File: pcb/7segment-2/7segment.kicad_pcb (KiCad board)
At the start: 2 copper layers, 26.4 x 21.8 mm, 3 parts, among them P1 CONN_02X05

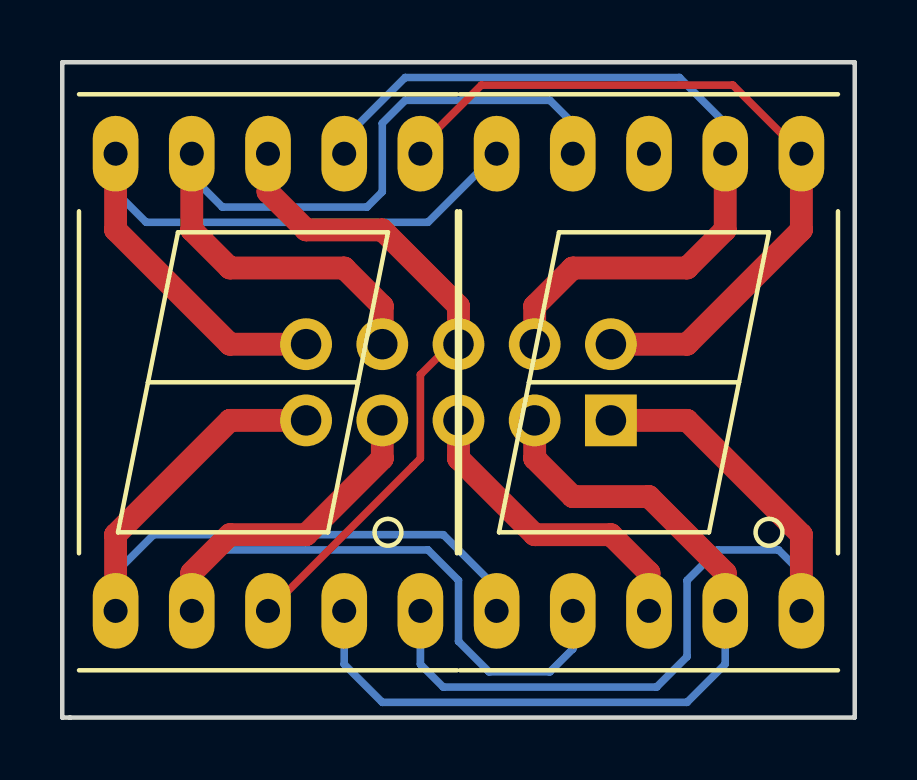
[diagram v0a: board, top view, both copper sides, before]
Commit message: added pinout to 7-segment pcb
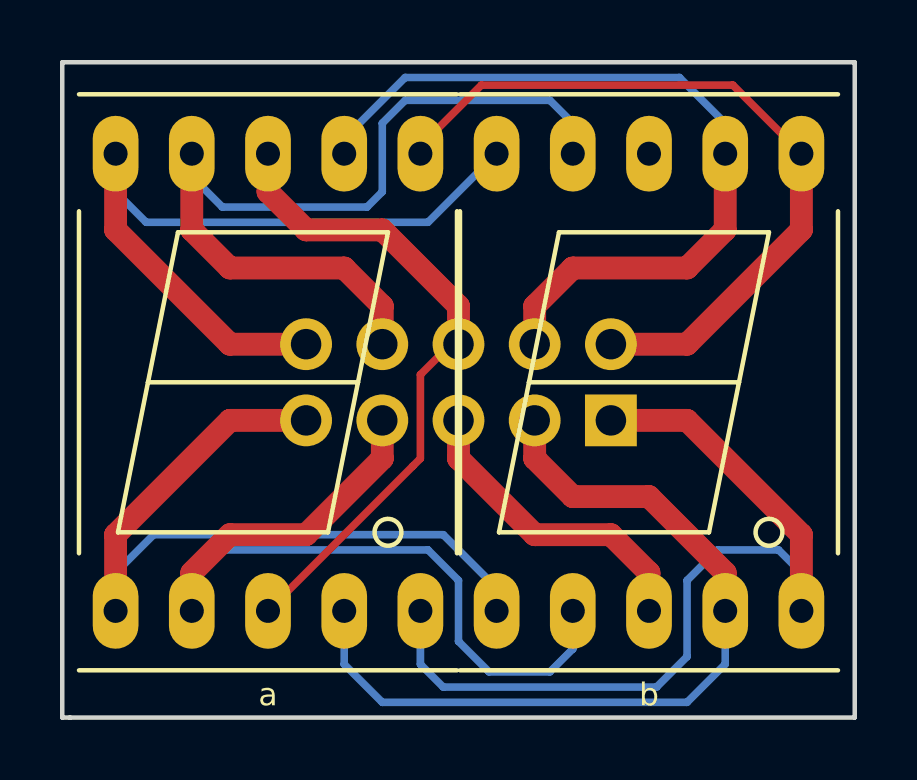
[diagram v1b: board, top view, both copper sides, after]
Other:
- board text added: "1 - dp"
- board text added: "10- g"
- board text added: "2 - b"
- board text added: "3 - c"
- board text added: "4 - a"
- board text added: "5 - se1"
- board text added: "6 - se2"
- board text added: "7 - d"
- board text added: "8 - f"
- board text added: "9 - e"
- board text added: "a"
- board text added: "b"
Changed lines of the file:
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@@
-(kicad_pcb (version 4) (host pcbnew 4.0.2+e4-6225~38~ubuntu14.04.1-stable)
+(kicad_pcb (version 4) (host pcbnew 4.0.4+e1-6308~48~ubuntu14.04.1-stable)
   (general
     (links 20)
     (no_connects 1)
-    (area 104.033095 93.396999 135.203001 117.115)
+    (area 104.108095 93.396999 135.203001 117.215)
     (thickness 1.6)
-    (drawings 5)
+    (drawings 17)
     (tracks 98)
     (zones 0)
@@
   )
   (setup
-    (last_trace_width 0.254)
+    (last_trace_width 0.25)
     (user_trace_width 0.254)
     (user_trace_width 0.508)
@@
     )
   )
+  (gr_text b (at 128.27 114.554) (layer F.SilkS)
+    (effects (font (size 0.762 0.762) (thickness 0.1905)))
+  )
+  (gr_text a (at 115.57 114.554) (layer F.SilkS)
+    (effects (font (size 0.762 0.762) (thickness 0.1905)))
+  )
+  (gr_text "10- g" (at 115.316 95.631) (layer B.SilkS)
+    (effects (font (size 1.016 1.016) (thickness 0.254)) (justify left mirror))
+  )
+  (gr_text "9 - e" (at 115.316 97.536) (layer B.SilkS)
+    (effects (font (size 1.016 1.016) (thickness 0.254)) (justify left mirror))
+  )
+  (gr_text "8 - f" (at 115.316 99.441) (layer B.SilkS)
+    (effects (font (size 1.016 1.016) (thickness 0.254)) (justify left mirror))
+  )
+  (gr_text "7 - d" (at 115.316 101.346) (layer B.SilkS)
+    (effects (font (size 1.016 1.016) (thickness 0.254)) (justify left mirror))
+  )
+  (gr_text "6 - se2" (at 115.316 103.251) (layer B.SilkS)
+    (effects (font (size 1.016 1.016) (thickness 0.254)) (justify left mirror))
+  )
+  (gr_text "5 - se1" (at 115.316 105.156) (layer B.SilkS)
+    (effects (font (size 1.016 1.016) (thickness 0.254)) (justify left mirror))
+  )
+  (gr_text "4 - a" (at 115.316 107.061) (layer B.SilkS)
+    (effects (font (size 1.016 1.016) (thickness 0.254)) (justify left mirror))
+  )
+  (gr_text "3 - c" (at 115.316 108.966) (layer B.SilkS)
+    (effects (font (size 1.016 1.016) (thickness 0.254)) (justify left mirror))
+  )
+  (gr_text "2 - b" (at 115.316 110.871) (layer B.SilkS)
+    (effects (font (size 1.016 1.016) (thickness 0.254)) (justify left mirror))
+  )
+  (gr_text "1 - dp" (at 115.316 112.776) (layer B.SilkS)
+    (effects (font (size 1.016 1.016) (thickness 0.254)) (justify left mirror))
+  )
   (gr_line (start 108.712 115.316) (end 108.712 93.472) (angle 90) (layer Edge.Cuts) (width 0.15))
   (gr_line (start 108.966 115.316) (end 108.712 115.316) (angle 90) (layer Edge.Cuts) (width 0.15))
@@
   (segment (start 116.84 109.22) (end 114.3 109.22) (width 0.762) (layer F.Cu) (net 2))
   (segment (start 119.38 106.68) (end 116.84 109.22) (width 0.762) (layer F.Cu) (net 2))
-  (via (at 115.57 111.76) (size 0.6) (drill 0.4) (layers F.Cu B.Cu) (net 3) (status C00000))
-  (segment (start 115.57 111.76) (end 120.396 106.934) (width 0.254) (layer F.Cu) (net 3) (status 400000))
-  (segment (start 120.65 103.886) (end 121.666 102.87) (width 0.254) (layer F.Cu) (net 3) (status 800000))
+  (via (at 115.57 111.76) (size 0.6) (drill 0.4) (layers F.Cu B.Cu) (net 3))
+  (segment (start 115.57 111.76) (end 120.396 106.934) (width 0.254) (layer F.Cu) (net 3))
+  (segment (start 120.65 103.886) (end 121.666 102.87) (width 0.254) (layer F.Cu) (net 3))
   (segment (start 120.65 106.68) (end 120.65 103.886) (width 0.254) (layer F.Cu) (net 3))
   (segment (start 120.396 106.934) (end 120.65 106.68) (width 0.254) (layer F.Cu) (net 3))
-  (segment (start 121.666 102.87) (end 121.92 102.87) (width 0.254) (layer F.Cu) (net 3) (status C00000))
+  (segment (start 121.666 102.87) (end 121.92 102.87) (width 0.254) (layer F.Cu) (net 3))
   (segment (start 121.92 102.87) (end 121.92 101.6) (width 0.762) (layer F.Cu) (net 3))
   (segment (start 115.57 97.79) (end 115.57 96.52) (width 0.762) (layer F.Cu) (net 3))
@@
   (segment (start 119.38 99.06) (end 116.84 99.06) (width 0.762) (layer F.Cu) (net 3))
   (segment (start 121.92 101.6) (end 119.38 99.06) (width 0.762) (layer F.Cu) (net 3))
-  (segment (start 118.11 111.76) (end 118.11 113.538) (width 0.254) (layer B.Cu) (net 4) (status 400000))
-  (segment (start 130.81 113.538) (end 130.81 111.76) (width 0.254) (layer B.Cu) (net 4) (status 800000))
+  (segment (start 118.11 111.76) (end 118.11 113.538) (width 0.254) (layer B.Cu) (net 4))
+  (segment (start 130.81 113.538) (end 130.81 111.76) (width 0.254) (layer B.Cu) (net 4))
   (segment (start 129.54 114.808) (end 130.81 113.538) (width 0.254) (layer B.Cu) (net 4))
   (segment (start 119.38 114.808) (end 129.54 114.808) (width 0.254) (layer B.Cu) (net 4))
@@
   (segment (start 125.73 107.95) (end 128.27 107.95) (width 0.762) (layer F.Cu) (net 4))
   (segment (start 124.46 106.68) (end 125.73 107.95) (width 0.762) (layer F.Cu) (net 4))
-  (segment (start 120.65 111.76) (end 120.65 113.538) (width 0.254) (layer B.Cu) (net 5) (status 400000))
-  (segment (start 133.35 110.49) (end 133.35 111.76) (width 0.254) (layer B.Cu) (net 5) (status 800000))
+  (segment (start 120.65 111.76) (end 120.65 113.538) (width 0.254) (layer B.Cu) (net 5))
+  (segment (start 133.35 110.49) (end 133.35 111.76) (width 0.254) (layer B.Cu) (net 5))
   (segment (start 132.588 109.728) (end 133.35 110.49) (width 0.254) (layer B.Cu) (net 5))
   (segment (start 130.556 109.728) (end 132.588 109.728) (width 0.254) (layer B.Cu) (net 5))
@@
   (segment (start 133.35 109.22) (end 133.35 111.76) (width 0.762) (layer F.Cu) (net 5))
   (segment (start 129.54 105.41) (end 133.35 109.22) (width 0.762) (layer F.Cu) (net 5))
-  (segment (start 120.65 96.52) (end 120.65 96.266) (width 0.254) (layer F.Cu) (net 6) (status C00000))
-  (segment (start 120.65 96.266) (end 122.682 94.234) (width 0.254) (layer F.Cu) (net 6) (status 400000))
+  (segment (start 120.65 96.52) (end 120.65 96.266) (width 0.254) (layer F.Cu) (net 6))
+  (segment (start 120.65 96.266) (end 122.682 94.234) (width 0.254) (layer F.Cu) (net 6))
   (segment (start 122.682 94.234) (end 131.064 94.234) (width 0.254) (layer F.Cu) (net 6))
-  (segment (start 131.064 94.234) (end 133.35 96.52) (width 0.254) (layer F.Cu) (net 6) (status 800000))
+  (segment (start 131.064 94.234) (end 133.35 96.52) (width 0.254) (layer F.Cu) (net 6))
   (segment (start 127 102.87) (end 129.54 102.87) (width 0.762) (layer F.Cu) (net 6))
   (segment (start 133.35 99.06) (end 133.35 96.52) (width 0.762) (layer F.Cu) (net 6))
   (segment (start 129.54 102.87) (end 133.35 99.06) (width 0.762) (layer F.Cu) (net 6))
-  (segment (start 118.11 96.52) (end 118.11 96.012) (width 0.254) (layer B.Cu) (net 7) (status C00000))
-  (segment (start 118.11 96.012) (end 120.142 93.98) (width 0.254) (layer B.Cu) (net 7) (status 400000))
+  (segment (start 118.11 96.52) (end 118.11 96.012) (width 0.254) (layer B.Cu) (net 7))
+  (segment (start 118.11 96.012) (end 120.142 93.98) (width 0.254) (layer B.Cu) (net 7))
   (segment (start 120.142 93.98) (end 129.286 93.98) (width 0.254) (layer B.Cu) (net 7))
-  (segment (start 129.286 93.98) (end 130.81 95.504) (width 0.254) (layer B.Cu) (net 7) (status 800000))
-  (segment (start 130.81 95.504) (end 130.81 96.52) (width 0.254) (layer B.Cu) (net 7) (status C00000))
+  (segment (start 129.286 93.98) (end 130.81 95.504) (width 0.254) (layer B.Cu) (net 7))
+  (segment (start 130.81 95.504) (end 130.81 96.52) (width 0.254) (layer B.Cu) (net 7))
   (segment (start 124.46 102.87) (end 124.46 101.6) (width 0.762) (layer F.Cu) (net 7))
   (segment (start 130.81 99.06) (end 130.81 96.52) (width 0.762) (layer F.Cu) (net 7))
@@
   (segment (start 125.73 100.33) (end 129.54 100.33) (width 0.762) (layer F.Cu) (net 7))
   (segment (start 124.46 101.6) (end 125.73 100.33) (width 0.762) (layer F.Cu) (net 7))
-  (segment (start 113.03 96.52) (end 113.03 97.282) (width 0.254) (layer B.Cu) (net 8) (status C00000))
-  (segment (start 113.03 97.282) (end 114.046 98.298) (width 0.254) (layer B.Cu) (net 8) (status 400000))
-  (segment (start 124.968 94.742) (end 125.73 95.504) (width 0.254) (layer B.Cu) (net 8) (status 800000))
+  (segment (start 113.03 96.52) (end 113.03 97.282) (width 0.254) (layer B.Cu) (net 8))
+  (segment (start 113.03 97.282) (end 114.046 98.298) (width 0.254) (layer B.Cu) (net 8))
+  (segment (start 124.968 94.742) (end 125.73 95.504) (width 0.254) (layer B.Cu) (net 8))
   (segment (start 120.142 94.742) (end 124.968 94.742) (width 0.254) (layer B.Cu) (net 8))
   (segment (start 119.38 95.504) (end 120.142 94.742) (width 0.254) (layer B.Cu) (net 8))
@@
   (segment (start 118.872 98.298) (end 119.38 97.79) (width 0.254) (layer B.Cu) (net 8))
   (segment (start 114.046 98.298) (end 118.872 98.298) (width 0.254) (layer B.Cu) (net 8))
-  (segment (start 125.73 95.504) (end 125.73 96.52) (width 0.254) (layer B.Cu) (net 8) (status C00000))
+  (segment (start 125.73 95.504) (end 125.73 96.52) (width 0.254) (layer B.Cu) (net 8))
   (segment (start 119.38 102.87) (end 119.38 101.6) (width 0.762) (layer F.Cu) (net 8))
   (segment (start 113.03 99.06) (end 113.03 96.52) (width 0.762) (layer F.Cu) (net 8))
@@
   (segment (start 118.11 100.33) (end 114.3 100.33) (width 0.762) (layer F.Cu) (net 8))
   (segment (start 119.38 101.6) (end 118.11 100.33) (width 0.762) (layer F.Cu) (net 8))
-  (segment (start 110.49 96.52) (end 110.49 97.79) (width 0.254) (layer B.Cu) (net 9) (status 400000))
-  (segment (start 120.904 98.806) (end 123.19 96.52) (width 0.254) (layer B.Cu) (net 9) (status 800000))
+  (segment (start 110.49 96.52) (end 110.49 97.79) (width 0.254) (layer B.Cu) (net 9))
+  (segment (start 120.904 98.806) (end 123.19 96.52) (width 0.254) (layer B.Cu) (net 9))
   (segment (start 111.506 98.806) (end 120.904 98.806) (width 0.254) (layer B.Cu) (net 9))
   (segment (start 110.49 97.79) (end 111.506 98.806) (width 0.254) (layer B.Cu) (net 9))
